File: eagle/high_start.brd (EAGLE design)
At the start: 100.1 x 80.8 mm, 34 parts, among them IC1 7805L, Q1 16Mhz, Q2 IRF510, Q3 IRF510, Q4 IRF510, U2 ATMEGA328P_PDIP

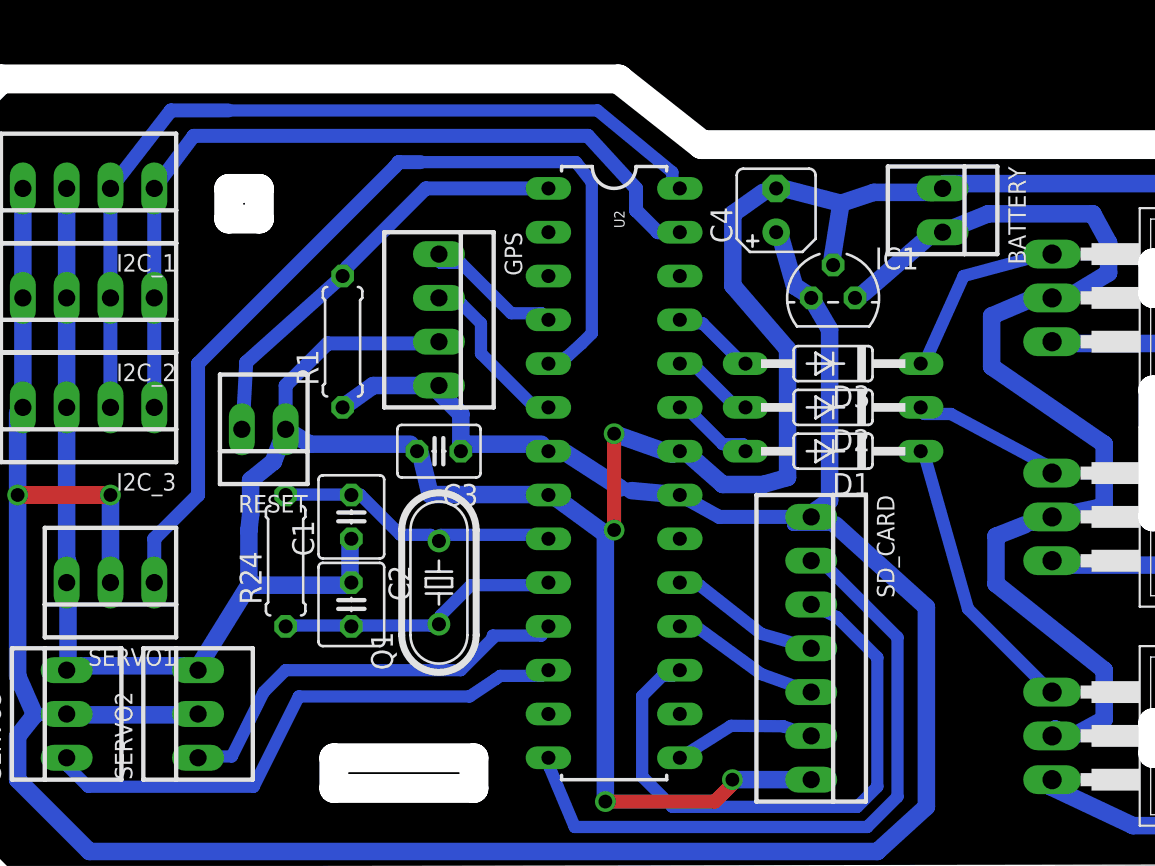
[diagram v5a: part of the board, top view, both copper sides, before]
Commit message: board tweaks and three servos into code
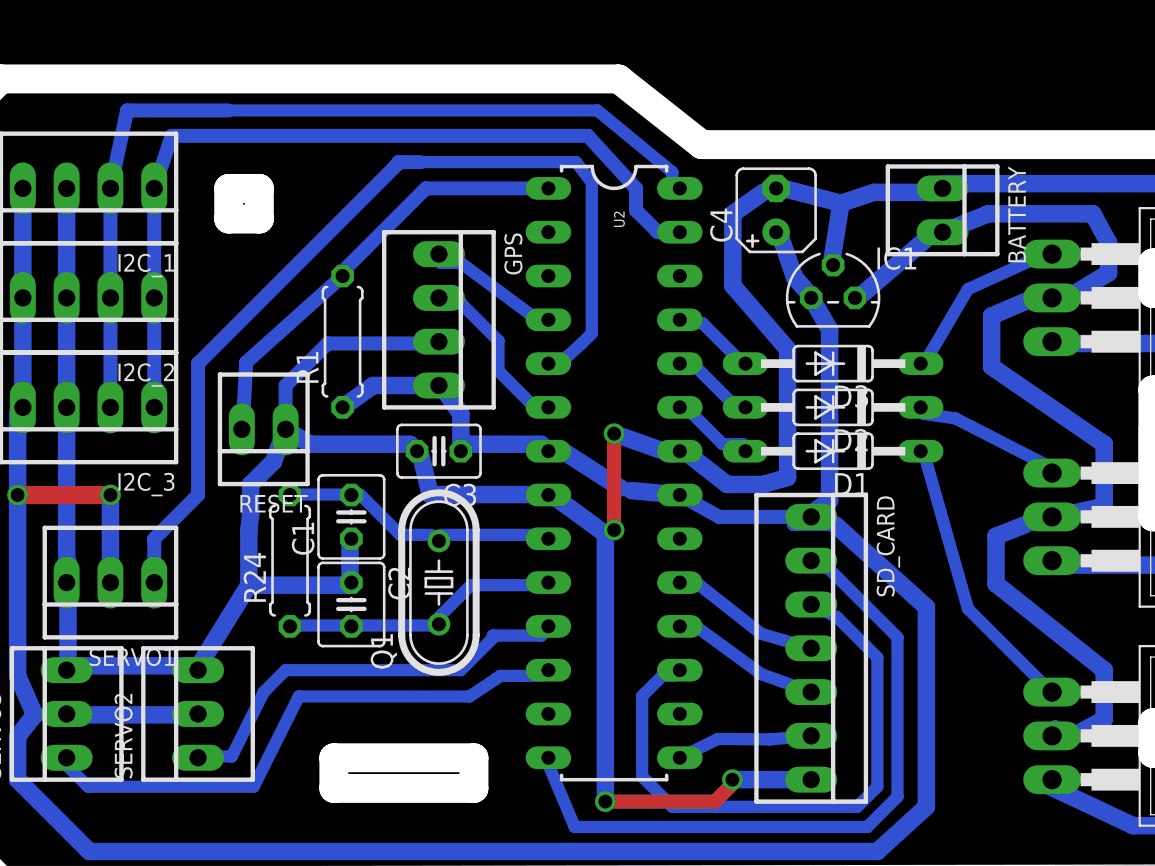
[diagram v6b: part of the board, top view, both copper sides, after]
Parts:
- moved R24 0.25 mm to (19.3, 17.8)
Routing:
- net N$1: track 49.9 -> 51.4 mm
- net N$2: track 47.8 -> 48.5 mm
- net N$14: track 11.1 -> 10.5 mm
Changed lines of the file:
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@@
 </element>
 <element name="R1" library="rcl" package="0207/7" value="10k" x="22.352" y="30.48" rot="R90"/>
-<element name="R24" library="rcl" package="0207/7" value="1M" x="19.05" y="17.78" rot="R90"/>
+<element name="R24" library="rcl" package="0207/7" value="1M" x="19.304" y="17.78" rot="R90"/>
 <element name="U2" library="SparkFun-DigitalIC" package="DIL28-3" value="ATMEGA328P_PDIP" x="38.1" y="22.86" rot="R270"/>
 <element name="RESET" library="con-molex" package="22-23-2021" value="22-23-2021" x="17.78" y="25.4" rot="R180">
@@
 <wire x1="23.368" y1="21.6154" x2="22.86" y2="21.59" width="0.7112" layer="16"/>
 <wire x1="22.7838" y1="21.6154" x2="19.2786" y2="21.6154" width="0.7112" layer="16"/>
-<wire x1="19.2786" y1="21.6154" x2="19.05" y2="21.59" width="0.7112" layer="16"/>
+<wire x1="19.2786" y1="21.6154" x2="19.304" y2="21.59" width="0.7112" layer="16"/>
 <wire x1="22.7838" y1="21.6154" x2="22.86" y2="21.59" width="0.7112" layer="16"/>
 <wire x1="28.0416" y1="19.2786" x2="33.8836" y2="19.2786" width="0.7112" layer="16"/>
@@
 <contactref element="R24" pad="1"/>
 <wire x1="22.7838" y1="14.0208" x2="19.2786" y2="14.0208" width="0.7112" layer="16"/>
-<wire x1="19.2786" y1="14.0208" x2="19.05" y2="13.97" width="0.7112" layer="16"/>
+<wire x1="19.2786" y1="14.0208" x2="19.304" y2="13.97" width="0.7112" layer="16"/>
 <wire x1="22.7838" y1="14.0208" x2="22.86" y2="13.97" width="0.7112" layer="16"/>
 <wire x1="23.368" y1="14.0208" x2="27.4574" y2="14.0208" width="0.7112" layer="16"/>
@@
 <contactref element="C4" pad="+"/>
 <wire x1="29.21" y1="26.289" x2="29.21" y2="24.5364" width="1.016" layer="16"/>
-<wire x1="28.0416" y1="27.4574" x2="29.21" y2="26.289" width="1.016" layer="16"/>
-<wire x1="28.0416" y1="27.4574" x2="27.94" y2="27.94" width="0.7112" layer="16"/>
+<wire x1="28.0416" y1="27.9654" x2="29.21" y2="26.289" width="1.016" layer="16"/>
+<wire x1="28.0416" y1="27.9654" x2="27.94" y2="27.94" width="0.7112" layer="16"/>
 <wire x1="29.21" y1="24.5364" x2="33.8836" y2="24.5364" width="1.016" layer="16"/>
 <wire x1="33.8836" y1="24.5364" x2="34.29" y2="24.13" width="0.7112" layer="16"/>
@@
 <wire x1="35.306" y1="24.0284" x2="34.4678" y2="24.0284" width="0.7112" layer="16"/>
 <wire x1="34.4678" y1="24.0284" x2="34.29" y2="24.13" width="0.7112" layer="16"/>
-<wire x1="48.5648" y1="33.7058" x2="49.5808" y2="33.0454" width="1.016" layer="16"/>
-<wire x1="47.752" y1="36.5506" x2="48.5648" y2="33.7058" width="1.016" layer="16"/>
+<wire x1="48.5648" y1="34.2138" x2="49.5808" y2="33.0454" width="1.016" layer="16"/>
+<wire x1="47.752" y1="36.5506" x2="48.5648" y2="34.2138" width="1.016" layer="16"/>
 <wire x1="49.5808" y1="33.0454" x2="49.53" y2="33.02" width="0.7112" layer="16"/>
 <wire x1="47.752" y1="36.5506" x2="47.498" y2="36.83" width="0.7112" layer="16"/>
@@
 <wire x1="48.1584" y1="22.606" x2="48.1584" y2="30.0482" width="1.016" layer="16"/>
 <wire x1="46.736" y1="22.1996" x2="48.1584" y2="22.606" width="1.016" layer="16"/>
-<wire x1="44.3992" y1="22.1996" x2="46.736" y2="22.1996" width="1.016" layer="16"/>
-<wire x1="42.3164" y1="24.0284" x2="44.3992" y2="22.1996" width="1.016" layer="16"/>
+<wire x1="44.6532" y1="22.1996" x2="46.736" y2="22.1996" width="1.016" layer="16"/>
+<wire x1="42.3164" y1="24.0284" x2="44.6532" y2="22.1996" width="1.016" layer="16"/>
 <wire x1="46.736" y1="39.1414" x2="47.498" y2="39.37" width="0.7112" layer="16"/>
 <wire x1="42.3164" y1="24.0284" x2="41.91" y2="24.13" width="0.7112" layer="16"/>
@@
 <wire x1="16.9164" y1="19.5326" x2="16.9164" y2="16.3576" width="1.016" layer="16"/>
 <wire x1="17.018" y1="20.447" x2="16.9164" y2="19.5326" width="1.016" layer="16"/>
-<wire x1="17.018" y1="22.4536" x2="17.018" y2="20.447" width="1.016" layer="16"/>
-<wire x1="18.3388" y1="23.5204" x2="17.018" y2="22.4536" width="1.016" layer="16"/>
+<wire x1="17.018" y1="22.1996" x2="17.018" y2="20.447" width="1.016" layer="16"/>
+<wire x1="18.3388" y1="23.5204" x2="17.018" y2="22.1996" width="1.016" layer="16"/>
 <wire x1="18.3388" y1="23.5204" x2="19.05" y2="25.4" width="1.016" layer="16"/>
 <wire x1="85.1916" y1="39.5478" x2="91.1352" y2="39.5478" width="1.016" layer="16"/>
@@
 <wire x1="15.7226" y1="43.8912" x2="37.1348" y2="43.8912" width="0.7112" layer="16"/>
 <wire x1="41.4782" y1="39.7256" x2="41.91" y2="39.37" width="0.7112" layer="16"/>
-<wire x1="15.7226" y1="43.8912" x2="12.3952" y2="43.8912" width="0.8128" layer="16"/>
-<wire x1="12.3952" y1="43.8912" x2="8.89" y2="39.37" width="0.8128" layer="16"/>
+<wire x1="15.7226" y1="43.8912" x2="9.8552" y2="43.8912" width="0.8128" layer="16"/>
+<wire x1="9.8552" y1="43.8912" x2="8.89" y2="39.37" width="0.8128" layer="16"/>
 <wire x1="8.89" y1="26.67" x2="8.89" y2="33.02" width="0.8128" layer="16"/>
 <wire x1="8.89" y1="33.02" x2="8.89" y2="39.37" width="0.8128" layer="16"/>
@@
 <wire x1="39.37" y1="38.1" x2="39.37" y2="39.37" width="0.8128" layer="16"/>
 <wire x1="39.37" y1="39.37" x2="36.576" y2="42.418" width="0.8128" layer="16"/>
-<wire x1="36.576" y1="42.418" x2="13.716" y2="42.418" width="0.8128" layer="16"/>
-<wire x1="13.716" y1="42.418" x2="11.43" y2="39.37" width="0.8128" layer="16"/>
+<wire x1="36.576" y1="42.418" x2="12.446" y2="42.418" width="0.8128" layer="16"/>
+<wire x1="12.446" y1="42.418" x2="11.43" y2="39.37" width="0.8128" layer="16"/>
 <wire x1="11.43" y1="39.37" x2="11.43" y2="33.02" width="0.8128" layer="16"/>
 <wire x1="11.43" y1="33.02" x2="11.43" y2="26.67" width="0.8128" layer="16"/>
@@
 <contactref element="U2" pad="4"/>
 <contactref element="GPS" pad="1"/>
-<wire x1="32.131" y1="32.131" x2="33.8836" y2="32.131" width="0.7112" layer="16"/>
-<wire x1="29.21" y1="35.052" x2="32.131" y2="32.131" width="0.7112" layer="16"/>
+<wire x1="33.147" y1="32.131" x2="33.8836" y2="31.623" width="0.7112" layer="16"/>
+<wire x1="29.21" y1="35.052" x2="33.147" y2="32.131" width="0.7112" layer="16"/>
 <wire x1="28.0416" y1="35.052" x2="29.21" y2="35.052" width="0.7112" layer="16"/>
-<wire x1="33.8836" y1="32.131" x2="34.29" y2="31.75" width="0.7112" layer="16"/>
+<wire x1="33.8836" y1="31.623" x2="34.29" y2="31.75" width="0.7112" layer="16"/>
 <wire x1="28.0416" y1="35.052" x2="27.94" y2="35.56" width="0.7112" layer="16"/>
 </signal>
@@
 <contactref element="GPS" pad="2"/>
 <wire x1="33.2994" y1="26.8732" x2="33.8836" y2="26.8732" width="0.7112" layer="16"/>
-<wire x1="30.3784" y1="29.7942" x2="33.2994" y2="26.8732" width="0.7112" layer="16"/>
-<wire x1="30.3784" y1="31.5468" x2="30.3784" y2="29.7942" width="0.7112" layer="16"/>
-<wire x1="29.21" y1="32.7152" x2="30.3784" y2="31.5468" width="0.7112" layer="16"/>
+<wire x1="31.3944" y1="28.7782" x2="33.2994" y2="26.8732" width="0.7112" layer="16"/>
+<wire x1="31.3944" y1="30.5308" x2="31.3944" y2="28.7782" width="0.7112" layer="16"/>
+<wire x1="29.21" y1="32.7152" x2="31.3944" y2="30.5308" width="0.7112" layer="16"/>
 <wire x1="28.0416" y1="32.7152" x2="29.21" y2="32.7152" width="0.7112" layer="16"/>
 <wire x1="33.8836" y1="26.8732" x2="34.29" y2="26.67" width="0.7112" layer="16"/>
@@
 <contactref element="SD_CARD" pad="6"/>
 <contactref element="U2" pad="15"/>
-<wire x1="44.8818" y1="8.2042" x2="42.0624" y2="6.4262" width="0.7112" layer="16"/>
-<wire x1="47.9044" y1="8.1788" x2="44.8818" y2="8.2042" width="0.7112" layer="16"/>
+<wire x1="44.1198" y1="7.4422" x2="42.0624" y2="6.4262" width="0.7112" layer="16"/>
+<wire x1="47.1424" y1="7.4168" x2="44.1198" y2="7.4422" width="0.7112" layer="16"/>
 <wire x1="42.0624" y1="6.4262" x2="41.91" y2="6.35" width="0.7112" layer="16"/>
-<wire x1="47.9044" y1="8.1788" x2="49.53" y2="7.62" width="0.7112" layer="16"/>
+<wire x1="47.1424" y1="7.4168" x2="49.53" y2="7.62" width="0.7112" layer="16"/>
 </signal>
 <signal name="N$12">
 <contactref element="Q3" pad="1"/>
 <contactref element="D2" pad="C"/>
-<wire x1="57.6326" y1="26.289" x2="56.0832" y2="26.289" width="0.7112" layer="16"/>
-<wire x1="63.0936" y1="23.368" x2="57.6326" y2="26.289" width="0.7112" layer="16"/>
+<wire x1="57.8866" y1="26.035" x2="56.0832" y2="26.289" width="0.7112" layer="16"/>
+<wire x1="63.0936" y1="23.368" x2="57.8866" y2="26.035" width="0.7112" layer="16"/>
 <wire x1="56.0832" y1="26.289" x2="55.88" y2="26.67" width="0.7112" layer="16"/>
 <wire x1="63.0936" y1="23.368" x2="63.5" y2="22.86" width="0.7112" layer="16"/>
@@
 <contactref element="Q4" pad="1"/>
 <contactref element="D3" pad="C"/>
-<wire x1="58.3692" y1="34.29" x2="56.0832" y2="29.21" width="0.7112" layer="16"/>
-<wire x1="63.0936" y1="35.56" x2="58.3692" y2="34.29" width="0.7112" layer="16"/>
+<wire x1="58.6232" y1="33.528" x2="56.0832" y2="29.21" width="0.7112" layer="16"/>
+<wire x1="63.0936" y1="35.56" x2="58.6232" y2="33.528" width="0.7112" layer="16"/>
 <wire x1="56.0832" y1="29.21" x2="55.88" y2="29.21" width="0.7112" layer="16"/>
 <wire x1="63.0936" y1="35.56" x2="63.5" y2="35.56" width="0.7112" layer="16"/>

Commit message: added airframe cam files to the repo
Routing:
- net GND: track 254.4 -> 252.5 mm
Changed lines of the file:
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@@
 <contactref element="SERVO3" pad="3"/>
 <contactref element="SERVO2" pad="3"/>
-<contactref element="IGN1" pad="1"/>
-<contactref element="IGN3" pad="1"/>
-<contactref element="IGN2" pad="1"/>
 <contactref element="LED1" pad="K"/>
 <contactref element="LED3" pad="K"/>
@@
 <wire x1="91.7194" y1="27.4574" x2="94.0562" y2="28.5242" width="1.016" layer="16"/>
 <wire x1="92.9894" y1="35.4076" x2="92.71" y2="35.56" width="0.7112" layer="16"/>
-<wire x1="91.7194" y1="27.4574" x2="91.44" y2="27.94" width="0.7112" layer="16"/>
 <wire x1="92.202" y1="13.8938" x2="92.7354" y2="10.3632" width="1.016" layer="16"/>
 <wire x1="92.202" y1="13.6906" x2="92.202" y2="13.8938" width="1.016" layer="16"/>
@@
 <wire x1="92.0496" y1="15.113" x2="92.202" y2="13.6906" width="1.016" layer="16"/>
 <wire x1="92.7354" y1="10.3632" x2="92.71" y2="10.16" width="0.7112" layer="16"/>
-<wire x1="91.7194" y1="15.1892" x2="91.44" y2="15.24" width="0.7112" layer="16"/>
 <wire x1="92.3036" y1="2.921" x2="91.7194" y2="2.921" width="0.7112" layer="16"/>
 <wire x1="94.0562" y1="3.4036" x2="92.3036" y2="2.921" width="1.016" layer="16"/>
 <wire x1="94.0562" y1="7.6962" x2="94.0562" y2="3.4036" width="1.016" layer="16"/>
 <wire x1="92.9894" y1="10.033" x2="94.0562" y2="7.6962" width="1.016" layer="16"/>
-<wire x1="91.7194" y1="2.921" x2="91.44" y2="2.54" width="0.7112" layer="16"/>
 <wire x1="92.9894" y1="10.033" x2="92.71" y2="10.16" width="0.7112" layer="16"/>
 <wire x1="94.0562" y1="19.9644" x2="92.9894" y2="22.3012" width="1.016" layer="16"/>
@@
 <wire x1="92.0496" y1="15.113" x2="94.0562" y2="16.3576" width="1.016" layer="16"/>
 <wire x1="92.9894" y1="22.3012" x2="92.71" y2="22.86" width="0.7112" layer="16"/>
-<wire x1="92.0496" y1="15.113" x2="91.44" y2="15.24" width="0.7112" layer="16"/>
 <wire x1="22.7838" y1="18.6944" x2="22.7838" y2="16.9418" width="1.016" layer="16"/>
 <wire x1="22.7838" y1="16.9418" x2="22.86" y2="16.51" width="0.7112" layer="16"/>
@@
 <via x="38.1" y="19.558" extent="1-16" drill="0.8" shape="square"/>
 <wire x1="38.1" y1="19.558" x2="37.592" y2="19.05" width="0.8128" layer="16"/>
+<contactref element="IGN1" pad="1"/>
+<contactref element="IGN2" pad="1"/>
+<contactref element="IGN3" pad="1"/>
+<wire x1="91.7194" y1="27.4574" x2="91.44" y2="27.94" width="0" layer="19" extent="16-16"/>
+<wire x1="91.44" y1="15.24" x2="91.7194" y2="15.1892" width="0" layer="19" extent="16-16"/>
+<wire x1="91.44" y1="2.54" x2="91.7194" y2="2.921" width="0" layer="19" extent="16-16"/>
 </signal>
 <signal name="N$1">
